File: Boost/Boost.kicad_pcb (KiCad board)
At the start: 2 copper layers, 19 parts, among them P1 CONN_01X02, P2 TST, P3 TST, P4 CONN_01X02, U1 TSP61087

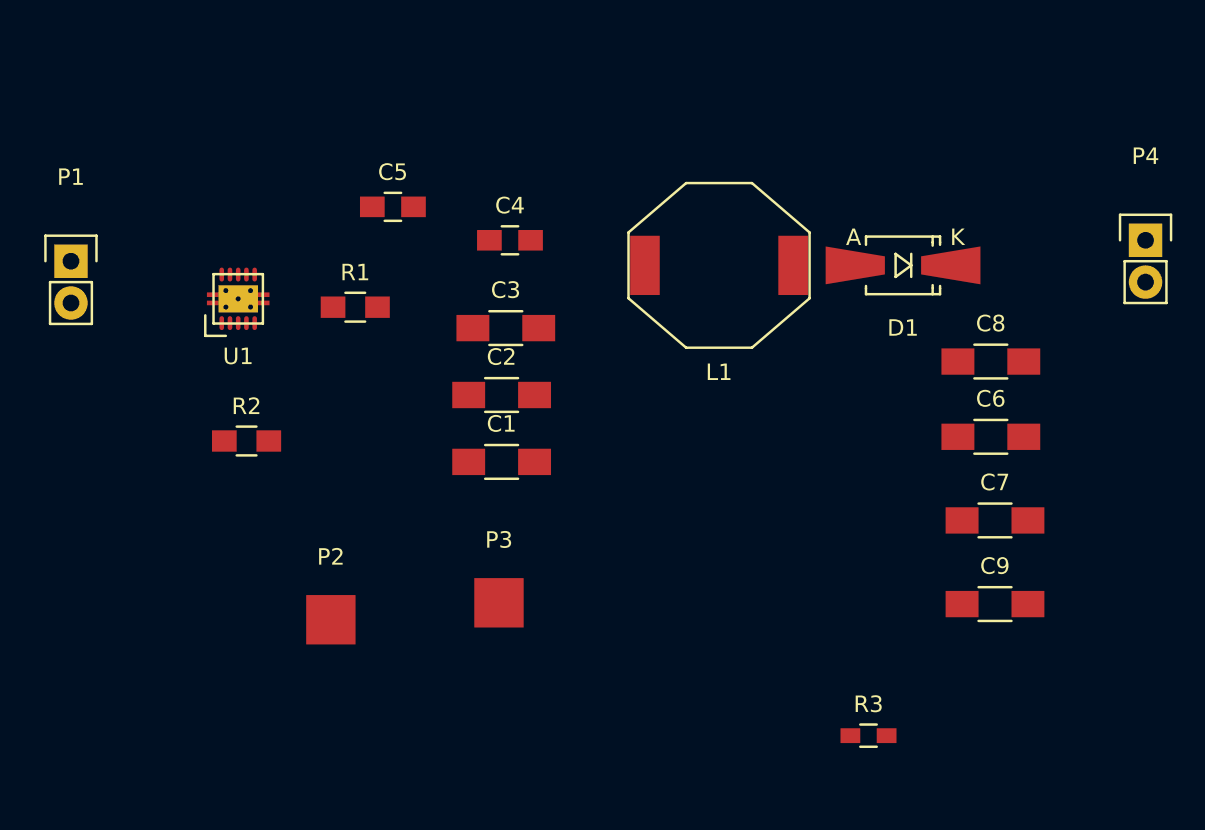
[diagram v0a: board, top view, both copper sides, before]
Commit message: Components in position for the layout
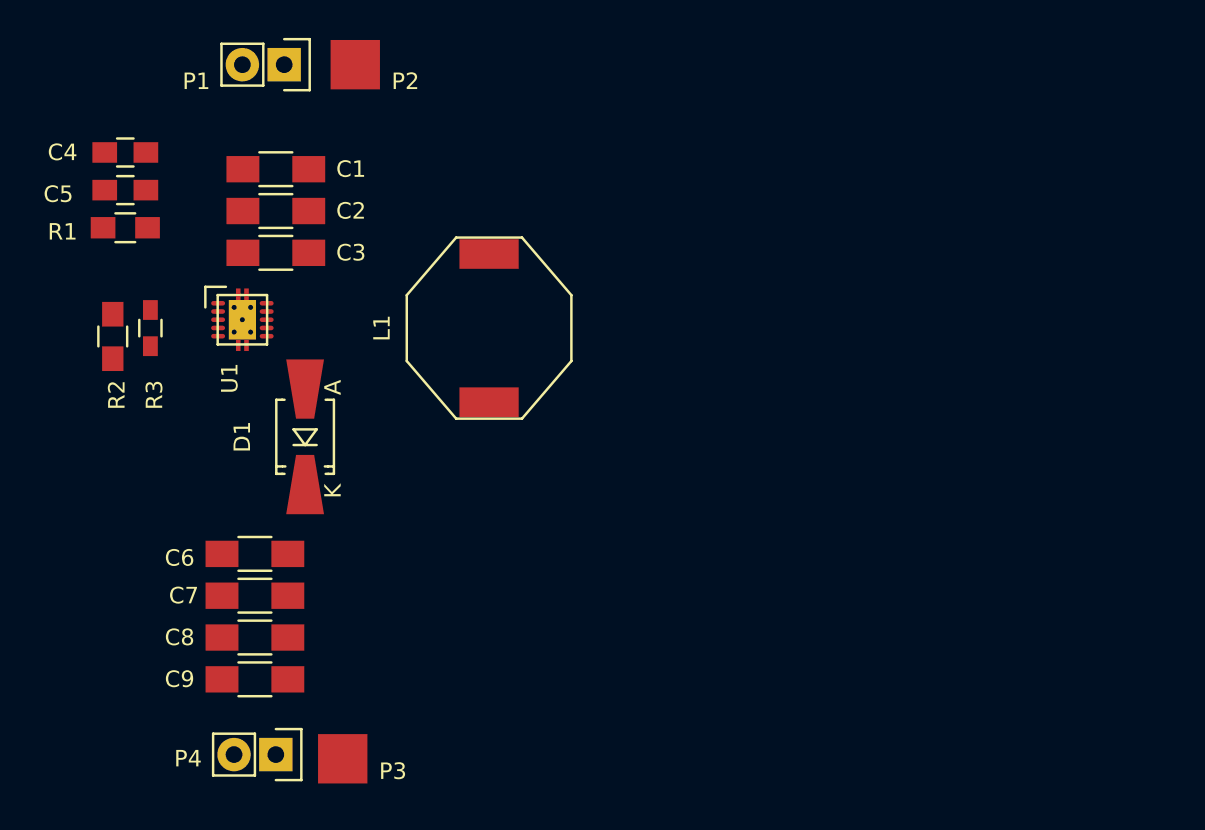
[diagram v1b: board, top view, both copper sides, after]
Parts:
- moved P4 61.4 mm to (159.3, 128.8), turned to 270 degrees
- moved R3 50.2 mm to (151.6, 102.9), turned to 270 degrees
- moved C8 47.7 mm to (158.0, 121.7), turned to 180 degrees
- moved C6 45.3 mm to (158.0, 116.6), turned to 180 degrees
- moved C7 45.2 mm to (158.0, 119.1), turned to 180 degrees
- moved C9 45.2 mm to (158.0, 124.2), turned to 180 degrees
- moved D1 37.8 mm to (161.0, 109.5), turned to 90 degrees
- moved P2 33.8 mm to (164.1, 86.9)
- moved C4 24.0 mm to (150.1, 92.2)
- moved C1 22.5 mm to (159.3, 93.2), turned to 180 degrees
- moved C2 17.7 mm to (159.3, 95.8), turned to 180 degrees
- moved P1 17.6 mm to (159.8, 86.9), turned to 270 degrees
- moved C5 16.3 mm to (150.1, 94.5)
- moved R1 14.8 mm to (150.1, 96.8), turned to 180 degrees
- moved C3 14.7 mm to (159.3, 98.3), turned to 180 degrees
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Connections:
- C9 pad 2: Net-(C9-Pad2) -> GND
- P3 pad 1: Net-(P3-Pad1) -> /Vout

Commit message: Added power planes for the layout
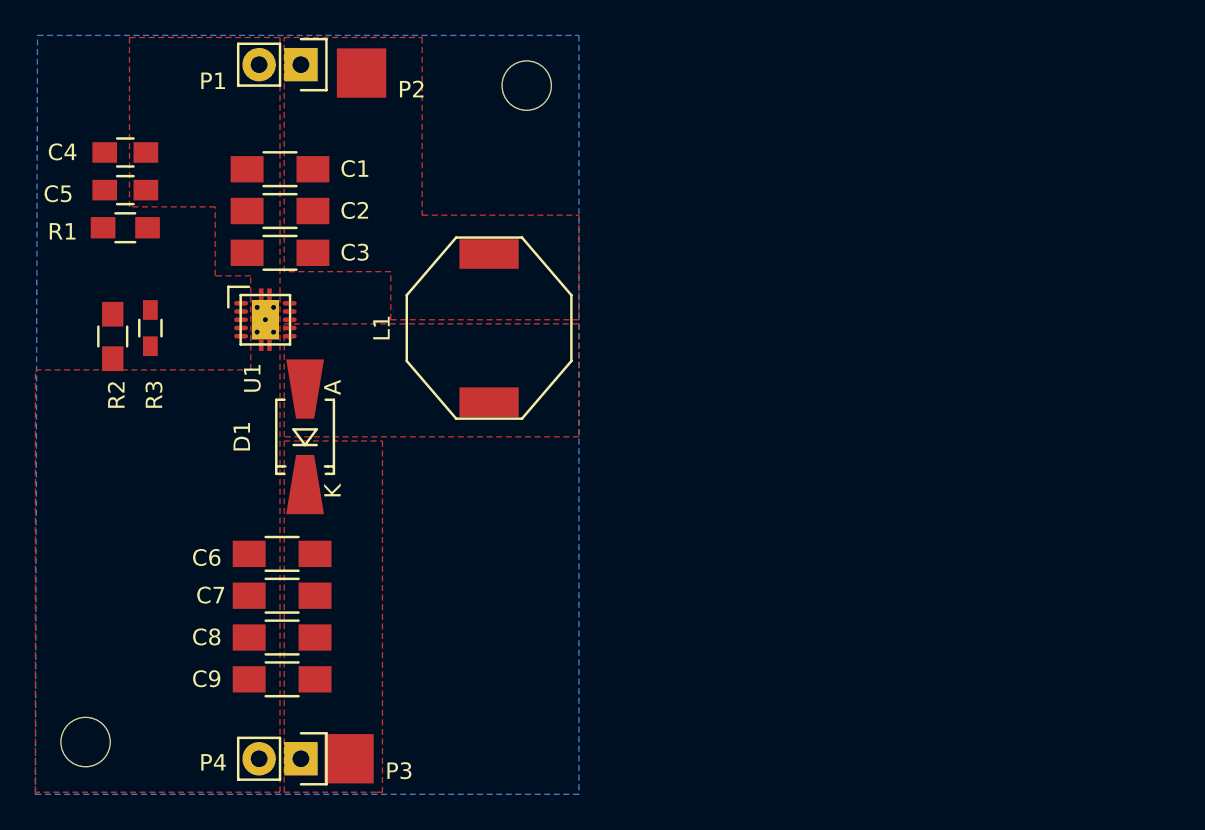
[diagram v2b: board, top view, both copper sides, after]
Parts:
- added REF**: MountingHole_3mm, Mounting_Holes:MountingHole_3mm, F.Cu at (174.5, 88.1)
- added REF**: MountingHole_3mm, Mounting_Holes:MountingHole_3mm, F.Cu at (147.7, 128.0)
- moved C6 1.65 mm to (159.6, 116.6)
- moved C7 1.65 mm to (159.6, 119.1)
- moved C8 1.65 mm to (159.6, 121.7)
- moved C9 1.65 mm to (159.6, 124.2)
- moved P4 1.55 mm to (160.8, 129.0)
- moved U1 1.40 mm to (158.6, 102.4)
- moved P1 1.02 mm to (160.8, 86.9)
- moved P2 0.64 mm to (164.5, 87.4)
- moved P3 0.38 mm to (163.7, 129.0)
- moved C1 0.25 mm to (159.5, 93.2)
- moved C2 0.25 mm to (159.5, 95.8)
- moved C3 0.25 mm to (159.5, 98.3)
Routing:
- added copper zone on F.Cu, net /Lin
- added copper zone on F.Cu, net /Lout
- added copper zone on F.Cu, net /Vout
- added copper zone on B.Cu, net GND
- added copper zone on F.Cu, net GND
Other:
- net class Default: clearance 0.2 -> 0.1524; trace_width 0.25 -> 0.1524; via_dia 0.6 -> 0.6858; via_drill 0.4 -> 0.3302
- rule trace_clearance: 0.2 -> 0.1524
- rule trace_min: 0.2 -> 0.1524
- rule via_min_drill: 0.3 -> 0.3302
- rule via_min_size: 0.4 -> 0.6858
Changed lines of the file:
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@@
   (general
     (links 46)
-    (no_connects 41)
-    (area 142.51281 81.759666 179.187 139.728333)
+    (no_connects 12)
+    (area 144.653 81.807266 179.1394 134.092733)
     (thickness 1.6)
     (drawings 0)
     (tracks 0)
     (zones 0)
-    (modules 19)
+    (modules 21)
     (nets 9)
   )
@@
   )
   (setup
-    (last_trace_width 0.25)
-    (trace_clearance 0.2)
-    (zone_clearance 0.508)
+    (last_trace_width 0.3048)
+    (user_trace_width 0.3048)
+    (user_trace_width 0.6096)
+    (trace_clearance 0.1524)
+    (zone_clearance 0.1524)
     (zone_45_only no)
-    (trace_min 0.2)
+    (trace_min 0.1524)
     (segment_width 0.2)
     (edge_width 0.15)
-    (via_size 0.6)
-    (via_drill 0.4)
-    (via_min_size 0.4)
-    (via_min_drill 0.3)
+    (via_size 0.6858)
+    (via_drill 0.3302)
+    (via_min_size 0.6858)
+    (via_min_drill 0.3302)
     (uvia_size 0.3)
     (uvia_drill 0.1)
     (uvias_allowed no)
-    (uvia_min_size 0.2)
-    (uvia_min_drill 0.1)
+    (uvia_min_size 0)
+    (uvia_min_drill 0)
     (pcb_text_width 0.3)
     (pcb_text_size 1.5 1.5)
@@
   (net 8 /FB)
   (net_class Default "This is the default net class."
-    (clearance 0.2)
-    (trace_width 0.25)
-    (via_dia 0.6)
-    (via_drill 0.4)
+    (clearance 0.1524)
+    (trace_width 0.1524)
+    (via_dia 0.6858)
+    (via_drill 0.3302)
     (uvia_dia 0.3)
     (uvia_drill 0.1)
@@
   )
   (module Capacitors_SMD:C_1206_HandSoldering (layer F.Cu)
-    (at 159.258 93.218 180)
+    (at 159.512 93.218 180)
     (descr "Capacitor SMD 1206, hand soldering")
     (tags "capacitor 1206")
@@
   )
   (module Capacitors_SMD:C_1206_HandSoldering (layer F.Cu)
-    (at 159.258 95.758 180)
+    (at 159.512 95.758 180)
     (descr "Capacitor SMD 1206, hand soldering")
     (tags "capacitor 1206")
@@
   )
   (module Capacitors_SMD:C_1206_HandSoldering (layer F.Cu)
-    (at 159.258 98.298 180)
+    (at 159.512 98.298 180)
     (descr "Capacitor SMD 1206, hand soldering")
     (tags "capacitor 1206")
@@
   )
   (module Capacitors_SMD:C_1206_HandSoldering (layer F.Cu)
-    (at 157.988 116.586 180)
+    (at 159.639 116.586 180)
     (descr "Capacitor SMD 1206, hand soldering")
     (tags "capacitor 1206")
@@
   )
   (module Capacitors_SMD:C_1206_HandSoldering (layer F.Cu)
-    (at 157.988 119.126 180)
+    (at 159.639 119.126 180)
     (descr "Capacitor SMD 1206, hand soldering")
     (tags "capacitor 1206")
@@
   )
   (module Capacitors_SMD:C_1206_HandSoldering (layer F.Cu)
-    (at 157.988 121.666 180)
+    (at 159.639 121.666 180)
     (descr "Capacitor SMD 1206, hand soldering")
     (tags "capacitor 1206")
@@
   )
   (module Capacitors_SMD:C_1206_HandSoldering (layer F.Cu)
-    (at 157.988 124.206 180)
+    (at 159.639 124.206 180)
     (descr "Capacitor SMD 1206, hand soldering")
     (tags "capacitor 1206")
@@
   )
   (module Pin_Headers:Pin_Header_Straight_1x02 (layer F.Cu)
-    (at 159.766 86.868 270)
+    (at 160.782 86.868 270)
     (descr "Through hole pin header")
     (tags "pin header")
@@
   )
   (module Measurement_Points:Measurement_Point_Square-SMD-Pad_Big (layer F.Cu)
-    (at 164.084 86.868)
+    (at 164.465 87.376)
     (descr "Mesurement Point, Square, SMD Pad,  3mm x 3mm,")
     (tags "Mesurement Point, Square, SMD Pad, 3mm x 3mm,")
@@
   )
   (module Measurement_Points:Measurement_Point_Square-SMD-Pad_Big (layer F.Cu)
-    (at 163.322 129.032)
+    (at 163.703 129.032)
     (descr "Mesurement Point, Square, SMD Pad,  3mm x 3mm,")
     (tags "Mesurement Point, Square, SMD Pad, 3mm x 3mm,")
@@
   )
   (module Pin_Headers:Pin_Header_Straight_1x02 (layer F.Cu)
-    (at 159.258 128.778 270)
+    (at 160.782 129.032 270)
     (descr "Through hole pin header")
     (tags "pin header")
@@
   )
   (module Boost-Footprints:TPS61087DSCR (layer F.Cu)
-    (at 157.226 102.362 270)
+    (at 158.623 102.362 270)
     (fp_text reference U1 (at 3.556 0.762 450) (layer F.SilkS)
       (effects (font (size 1 1) (thickness 0.15)))
@@
       (net 2 GND))
   )
+  (module Mounting_Holes:MountingHole_3mm (layer F.Cu)
+    (at 174.498 88.138)
+    (descr "Mounting hole, Befestigungsbohrung, 3mm, No Annular, Kein Restring,")
+    (tags "Mounting hole, Befestigungsbohrung, 3mm, No Annular, Kein Restring,")
+    (fp_text reference REF** (at 0 -4.0005) (layer F.SilkS) hide
+      (effects (font (size 1 1) (thickness 0.15)))
+    )
+    (fp_text value MountingHole_3mm (at 1.00076 5.00126) (layer F.Fab)
+      (effects (font (size 1 1) (thickness 0.15)))
+    )
+    (fp_circle (center 0 0) (end 3 0) (layer Cmts.User) (width 0.381))
+    (pad 1 thru_hole circle (at 0 0) (size 3 3) (drill 3) (layers))
+  )
+  (module Mounting_Holes:MountingHole_3mm (layer F.Cu)
+    (at 147.701 128.016)
+    (descr "Mounting hole, Befestigungsbohrung, 3mm, No Annular, Kein Restring,")
+    (tags "Mounting hole, Befestigungsbohrung, 3mm, No Annular, Kein Restring,")
+    (fp_text reference REF** (at 0 -4.0005) (layer F.SilkS) hide
+      (effects (font (size 1 1) (thickness 0.15)))
+    )
+    (fp_text value MountingHole_3mm (at 1.00076 5.00126) (layer F.Fab)
+      (effects (font (size 1 1) (thickness 0.15)))
+    )
+    (fp_circle (center 0 0) (end 3 0) (layer Cmts.User) (width 0.381))
+    (pad 1 thru_hole circle (at 0 0) (size 3 3) (drill 3) (layers))
+  )
+  (zone (net 5) (net_name /Vout) (layer F.Cu) (hatch edge 0.508)
+    (connect_pads yes (clearance 0.1524))
+    (min_thickness 0.254)
+    (fill yes (arc_segments 16) (thermal_gap 0.508) (thermal_bridge_width 0.508))
+    (polygon
+      (pts
+        (xy 165.354 131.064) (xy 159.766 131.064) (xy 159.766 109.728) (xy 165.735 109.728) (xy 165.735 131.064)
+      )
+    )
+  )
+  (zone (net 6) (net_name /Lout) (layer F.Cu) (hatch edge 0.508)
+    (connect_pads yes (clearance 0.1524))
+    (min_thickness 0.254)
+    (fill yes (arc_segments 16) (thermal_gap 0.508) (thermal_bridge_width 0.508))
+    (polygon
+      (pts
+        (xy 177.673 109.474) (xy 159.766 109.474) (xy 159.766 102.616) (xy 177.673 102.616) (xy 177.673 109.474)
+      )
+    )
+  )
+  (zone (net 1) (net_name /Lin) (layer F.Cu) (hatch edge 0.508)
+    (connect_pads yes (clearance 0.1524))
+    (min_thickness 0.254)
+    (fill yes (arc_segments 16) (thermal_gap 0.508) (thermal_bridge_width 0.508))
+    (polygon
+      (pts
+        (xy 168.148 96.012) (xy 177.673 96.012) (xy 177.673 102.362) (xy 166.243 102.362) (xy 166.243 99.441)
+        (xy 159.766 99.441) (xy 159.766 85.217) (xy 168.148 85.217) (xy 168.148 96.012)
+      )
+    )
+  )
+  (zone (net 2) (net_name GND) (layer F.Cu) (hatch edge 0.508)
+    (connect_pads yes (clearance 0.1524))
+    (min_thickness 0.254)
+    (fill yes (arc_segments 16) (thermal_gap 0.508) (thermal_bridge_width 0.508))
+    (polygon
+      (pts
+        (xy 159.512 131.064) (xy 144.653 131.064) (xy 144.653 105.41) (xy 157.734 105.41) (xy 157.734 99.695)
+        (xy 155.575 99.695) (xy 155.575 95.504) (xy 150.368 95.504) (xy 150.368 85.217) (xy 159.512 85.217)
+        (xy 159.512 131.064)
+      )
+    )
+  )
+  (zone (net 2) (net_name GND) (layer B.Cu) (hatch edge 0.508)
+    (connect_pads yes (clearance 0.1524))
+    (min_thickness 0.254)
+    (fill yes (arc_segments 16) (thermal_gap 0.508) (thermal_bridge_width 0.508))
+    (polygon
+      (pts
+        (xy 177.673 131.191) (xy 144.653 131.191) (xy 144.78 85.09) (xy 177.673 85.09) (xy 177.673 131.191)
+      )
+    )
+  )
 )
